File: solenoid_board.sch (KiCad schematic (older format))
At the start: 37 parts, among them J1 INPUT_ARRAY, J2 MCU_LEFT_LEGS, J3 MCU_RIGHT_LEGS, J4 Solenoid_PWR_Supply, J5 CAN_BUS, J6 SOLENOID_HEADER, Q1 PHP79NQ08LT, Q2 PHP79NQ08LT, Q3 PHP79NQ08LT, Q4 PHP79NQ08LT, Q5 PHP79NQ08LT, Q6 PHP79NQ08LT, U1 MCP2517FD-xSL, U2 CD4072B, U3 CD4072B, U4 MCP2542FDxMF, U5 74HC165, U6 74HC165, Y1 Crystal

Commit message: Swap to RS485, pre-PCB layout
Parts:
- removed C1, C2: 22pF, Capacitor_SMD:C_2010_5025Metric_Pad1.52x2.65mm_HandSolder, symbol Device:C
- removed C3, C4, C5: 0.1nF, Capacitor_SMD:C_2010_5025Metric_Pad1.52x2.65mm_HandSolder, symbol Device:C
- removed D1, D2, D3, D4, D5, D6: 1N4007, Diode_THT:D_DO-41_SOD81_P10.16mm_Horizontal, symbol Diode:1N4007
- removed J1: INPUT_ARRAY, Connector_PinHeader_2.54mm:PinHeader_1x12_P2.54mm_Vertical, symbol Connector_Generic:Conn_01x12
- removed J5: CAN_BUS, TerminalBlock:TerminalBlock_bornier-2_P5.08mm, symbol Connector_Generic:Conn_01x02
- removed J6: SOLENOID_HEADER, Connector_PinHeader_2.54mm:PinHeader_1x06_P2.54mm_Vertical, symbol Connector_Generic:Conn_01x06
- removed U1: MCP2517FD-xSL, Package_SO:SOIC-14_3.9x8.7mm_P1.27mm, symbol Interface_CAN_LIN:MCP2517FD-xSL
- removed U2, U3: CD4072B, CD4072BM96:CD4072BM96, symbol LOGIC_ICs:CD4072B
- removed U4: MCP2542FDxMF, Package_DFN_QFN:DFN-8-1EP_3x3mm_P0.65mm_EP1.55x2.4mm, symbol Interface_CAN_LIN:MCP2542FDxMF
- removed Y1: Crystal, ECS200205PXTR:XTAL_ECS-200-20-5PX-TR, symbol Device:Crystal
- added J1, J10, J11, J7, J8, J9: Screw_Terminal_01x02, TerminalBlock:TerminalBlock_bornier-2_P5.08mm, symbol Connector:Screw_Terminal_01x02
- added J5: RJ45, Connector_RJ:RJ45_Pulse_JK0654219NL_Horizontal, symbol Connector:RJ45
- added J6: Screw_Terminal_01x06, TerminalBlock:TerminalBlock_bornier-6_P5.08mm, symbol Connector:Screw_Terminal_01x06
- added R8: 10, Resistor_SMD:R_2010_5025Metric_Pad1.52x2.65mm_HandSolder, symbol Device:R
- added R9: 10k, Resistor_SMD:R_2010_5025Metric_Pad1.52x2.65mm_HandSolder, symbol Device:R
- added U1: CDSOT23-SM712, CDSOT23-SM712:CDSOT23-SM712, symbol Protection_ICs:CDSOT23-SM712
- added U4: SN65HVD72DR, sn65hvd72:SN65HVD72DR, symbol Interface_RS485:SN65HVD72DR
- R1: value 120 -> 10
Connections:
- net labels removed: RXCAN, TXCAN
- wire segments 71 -> 63
- no-connect marks 14 -> 22

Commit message: COMPLETE ROUTING!!!
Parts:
- removed R9: 10k, Resistor_SMD:R_2010_5025Metric_Pad1.52x2.65mm_HandSolder, symbol Device:R
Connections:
- net D10: now also R4.2; no longer R5.2
- net D11: now also R3.2; no longer R6.2
- net D12: now also R2.2; no longer R7.2
- net D13: no longer J1.1 (Pin_1), J1.2 (Pin_2), J10.1 (Pin_1), J10.2 (Pin_2), J11.1 (Pin_1), J11.2 (Pin_2), J7.1 (Pin_1), J7.2 (Pin_2), J8.1 (Pin_1), J8.2 (Pin_2), J9.1 (Pin_1), J9.2 (Pin_2), U5.11 (D0), U5.12 (D1), U5.13 (D2), U5.14 (D3), U5.3 (D4), U5.4 (D5), U5.5 (D6), U5.6 (D7), U6.11 (D0), U6.12 (D1), U6.13 (D2), U6.14 (D3)
- net D5: now also R7.2; no longer R2.2
- net D6: now also R6.2; no longer R3.2
- net D9: now also R5.2; no longer R4.2
- net RJ45_4: now reaches R1.1, U4.6 (A)
- net RJ45_4: now also J5.4; no longer J5.5
- net RJ45_5: now reaches R8.1, U4.7 (B)
- net RJ45_5: now also J5.5; no longer J5.4
- new net INP0_0: J1.1 (Pin_1), U5.11 (D0)
- new net INP0_1: J1.2 (Pin_2), U5.12 (D1)
- new net INP1_0: J7.1 (Pin_1), U5.13 (D2)
- new net INP1_1: J7.2 (Pin_2), U5.14 (D3)
- new net INP2_0: J8.1 (Pin_1), U5.3 (D4)
- new net INP2_1: J8.2 (Pin_2), U5.4 (D5)
- new net INP3_0: J9.1 (Pin_1), U5.5 (D6)
- new net INP3_1: J9.2 (Pin_2), U5.6 (D7)
- new net INP4_0: J10.1 (Pin_1), U6.11 (D0)
- new net INP4_1: J10.2 (Pin_2), U6.12 (D1)
- new net INP5_0: J11.1 (Pin_1), U6.13 (D2)
- new net INP5_1: J11.2 (Pin_2), U6.14 (D3)
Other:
- moved on the sheet: U5, U6

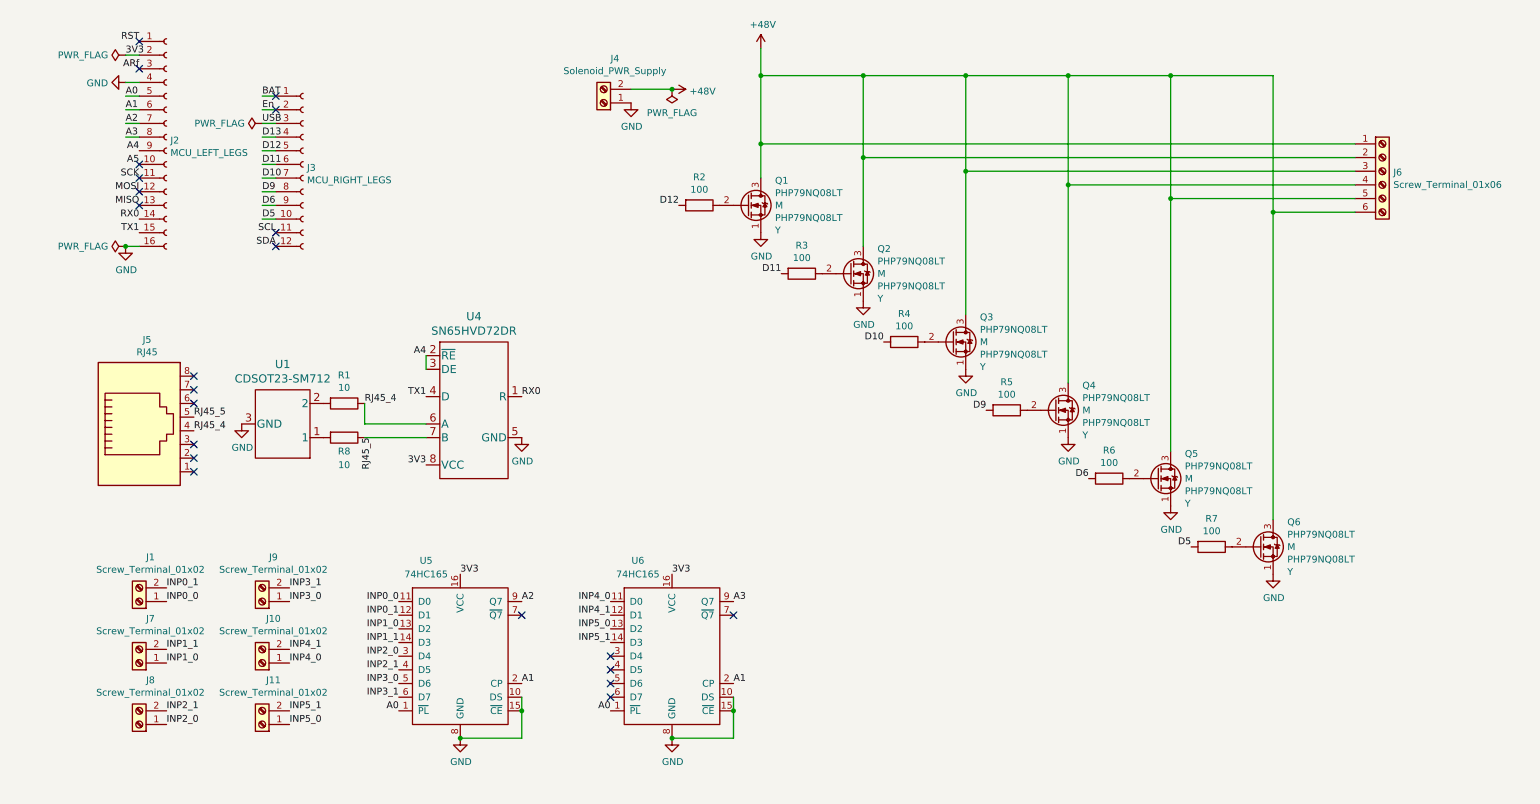
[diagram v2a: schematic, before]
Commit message: update schematic and netlist, fixing traces
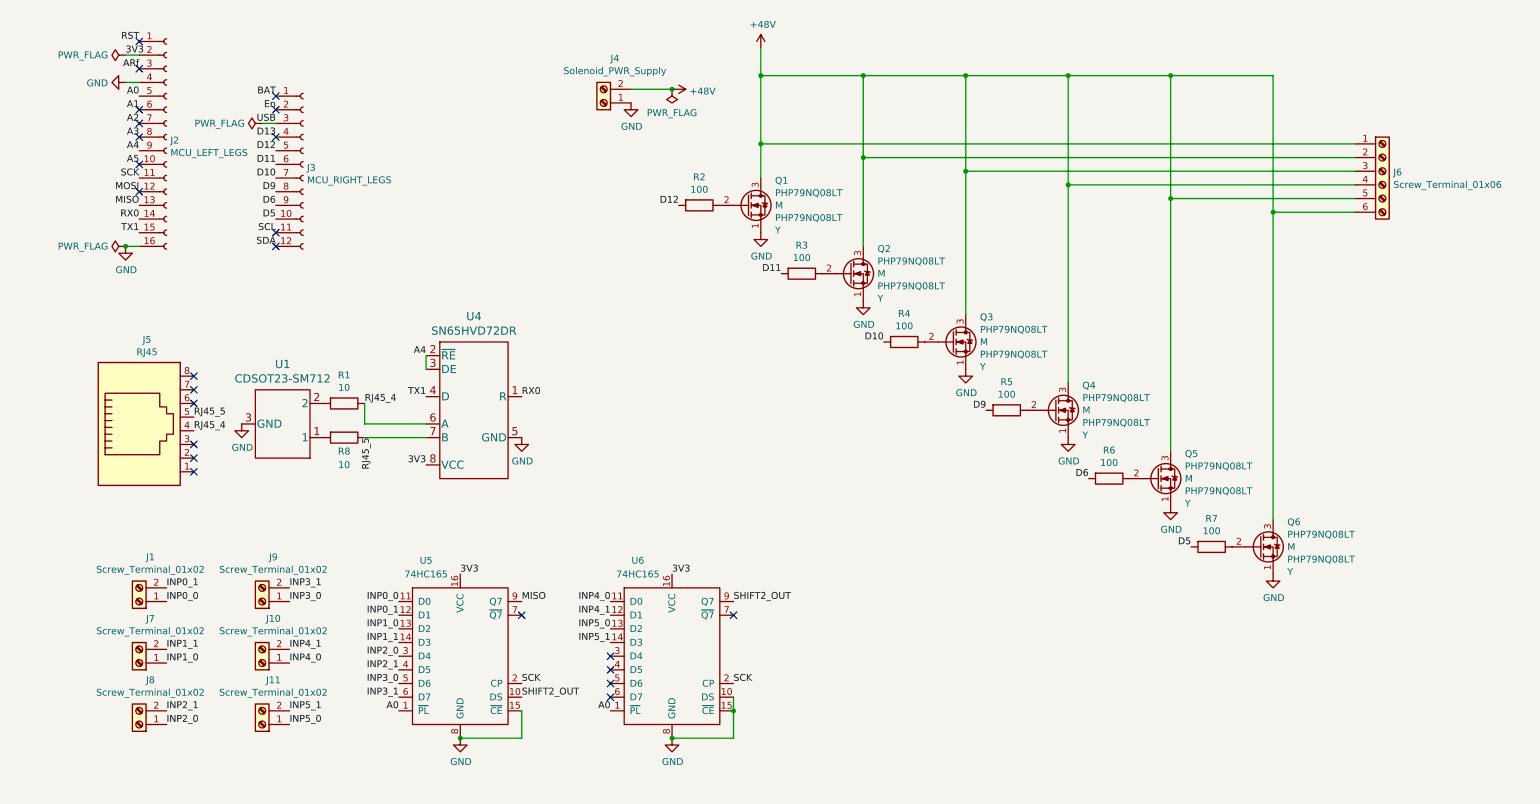
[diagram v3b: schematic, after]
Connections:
- net A1: no longer U5.2 (CP), U6.2 (CP)
- net A2: no longer U5.9 (Q7)
- net A3: no longer U6.9 (Q7)
- net GND: no longer U5.10 (DS)
- net MISO: now also U5.9 (Q7)
- net SCK: now also U5.2 (CP), U6.2 (CP)
- new net SHIFT2_OUT: U5.10 (DS), U6.9 (Q7)
- no-connect marks 22 -> 24
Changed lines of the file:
@@
 Wire Wire Line
 	1200 1000 1100 1000
-Wire Wire Line
-	1200 1100 1100 1100
-Wire Wire Line
-	1200 1200 1100 1200
 Text Label 1200 700  2    50   ~ 0
 RST
@@
 Text Label 1200 900  2    50   ~ 0
 ARf
-Text Label 1100 1100 0    50   ~ 0
+Text Label 1200 1100 2    50   ~ 0
 A0
-Text Label 1100 1200 0    50   ~ 0
+Text Label 1200 1200 2    50   ~ 0
 A1
 Wire Wire Line
-	1200 1300 1100 1300
-Wire Wire Line
-	1200 1400 1100 1400
-Wire Wire Line
 	1200 2200 1100 2200
-Text Label 1100 1300 0    50   ~ 0
+Text Label 1200 1300 2    50   ~ 0
 A2
-Text Label 1100 1400 0    50   ~ 0
-A3
 Text Label 1200 1500 2    50   ~ 0
 A4
@@
 $EndComp
 Wire Wire Line
-	2200 1100 2100 1100
-Wire Wire Line
-	2200 1200 2100 1200
-Wire Wire Line
 	2200 1300 2100 1300
-Wire Wire Line
-	2200 1400 2100 1400
-Wire Wire Line
-	2200 1500 2100 1500
-Wire Wire Line
-	2200 1600 2100 1600
-Wire Wire Line
-	2200 1700 2100 1700
-Wire Wire Line
-	2200 1800 2100 1800
-Wire Wire Line
-	2200 1900 2100 1900
-Wire Wire Line
-	2200 2000 2100 2000
-Text Label 2100 1100 0    50   ~ 0
+Text Label 2200 1100 2    50   ~ 0
 BAT
-Text Label 2100 1200 0    50   ~ 0
+Text Label 2200 1200 2    50   ~ 0
 En
-Text Label 2100 1300 0    50   ~ 0
+Text Label 2200 1300 2    50   ~ 0
 USB
-Text Label 2100 1400 0    50   ~ 0
-D13
-Text Label 2100 1500 0    50   ~ 0
+Text Label 2200 1500 2    50   ~ 0
 D12
-Text Label 2100 1600 0    50   ~ 0
+Text Label 2200 1600 2    50   ~ 0
 D11
-Text Label 2100 1700 0    50   ~ 0
+Text Label 2200 1700 2    50   ~ 0
 D10
-Text Label 2100 1800 0    50   ~ 0
+Text Label 2200 1800 2    50   ~ 0
 D9
-Text Label 2100 1900 0    50   ~ 0
+Text Label 2200 1900 2    50   ~ 0
 D6
-Text Label 2100 2000 0    50   ~ 0
+Text Label 2200 2000 2    50   ~ 0
 D5
 Text Label 2200 2100 2    50   ~ 0
@@
 Text Label 3100 5400 2    50   ~ 0
 INP3_0
-Text Label 4000 4800 0    50   ~ 0
-A2
-Wire Wire Line
-	4000 5500 4000 5600
 Text Label 3100 5500 2    50   ~ 0
 INP3_1
@@
 A0
 Text Label 4000 5400 0    50   ~ 0
-A1
+SCK
 $Comp
 L LOGIC_ICs:74HC165 U6
@@
 A0
 Text Label 5550 5400 0    50   ~ 0
-A1
+SCK
 Text Label 5550 4800 0    50   ~ 0
-A3
+SHIFT2_OUT
 Wire Wire Line
 	5550 5500 5550 5600
@@
 Wire Wire Line
 	4000 5800 3550 5800
-Connection ~ 4000 5600
 Connection ~ 3550 5800
 $Comp
@@
 Text Label 4000 3300 0    50   ~ 0
 RX0
-NoConn ~ 1200 1700
 NoConn ~ 1200 1800
-NoConn ~ 1200 1900
 Text Label 3300 3300 2    50   ~ 0
 TX1
@@
 Text Label 2900 3600 3    50   ~ 0
 RJ45_5
+Text Label 4000 5500 0    50   ~ 0
+SHIFT2_OUT
+Text Label 4000 4800 0    50   ~ 0
+MISO
+Text Label 1200 1400 2    50   ~ 0
+A3
+NoConn ~ 1200 1400
+NoConn ~ 1200 1300
+NoConn ~ 1200 1200
+NoConn ~ 2200 1400
+Text Label 2200 1400 2    50   ~ 0
+D13
 $EndSCHEMATC

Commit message: Finish routing
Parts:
- added J12: Screw_Terminal_01x06, TerminalBlock:TerminalBlock_bornier-6_P5.08mm, symbol Connector:Screw_Terminal_01x06
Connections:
- net +48V: now also J12.1 (Pin_1), J12.3 (Pin_3), J12.5 (Pin_5); no longer J6.2 (Pin_2), J6.4 (Pin_4), J6.6 (Pin_6), Q1.3 (D), Q2.3 (D), Q3.3 (D), Q4.3 (D), Q5.3 (D), Q6.3 (D)
- new net: J6.2 (Pin_2), Q1.3 (D)
- new net: J6.4 (Pin_4), Q2.3 (D)
- new net: J6.6 (Pin_6), Q3.3 (D)
- new net: J12.2 (Pin_2), Q4.3 (D)
- new net: J12.4 (Pin_4), Q5.3 (D)
- new net: J12.6 (Pin_6), Q6.3 (D)
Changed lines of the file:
@@
 Wire Wire Line
 	5750 950  5750 750
-Wire Wire Line
-	5750 1450 5750 1700
-Connection ~ 5750 1450
 $Comp
 L MOSFETs:PHP79NQ08LT Q2
@@
 $EndComp
 Wire Wire Line
-	6500 1550 6500 2200
-Connection ~ 6500 1550
-Wire Wire Line
-	7250 1650 7250 2700
-Connection ~ 7250 1650
-Wire Wire Line
-	8000 1750 8000 3200
-Connection ~ 8000 1750
-Wire Wire Line
 	5750 1450 10100 1450
-Wire Wire Line
-	6500 1550 10100 1550
-Wire Wire Line
-	7250 1650 10100 1650
-Wire Wire Line
-	8000 1750 10100 1750
 $Comp
 L Device:R R6
@@
 	1    0    0    -1
 $EndComp
-Wire Wire Line
-	8750 1850 10100 1850
-Wire Wire Line
-	8750 1850 8750 3700
-Connection ~ 8750 1850
-Wire Wire Line
-	10100 1950 9500 1950
-Connection ~ 9500 1950
-Wire Wire Line
-	9500 1950 9500 4200
 Text Label 5900 2400 2    50   ~ 0
 D11
@@
 	5750 950  5750 1450
 Connection ~ 5750 950
-Wire Wire Line
-	6500 950  6500 1550
 Connection ~ 6500 950
 Wire Wire Line
 	6500 950  7250 950
-Wire Wire Line
-	7250 950  7250 1650
 Connection ~ 7250 950
 Wire Wire Line
 	7250 950  8000 950
-Wire Wire Line
-	8000 950  8000 1750
 Connection ~ 8000 950
 Wire Wire Line
 	8000 950  8750 950
-Wire Wire Line
-	8750 950  8750 1850
 Connection ~ 8750 950
 Wire Wire Line
 	8750 950  9500 950
-Wire Wire Line
-	9500 950  9500 1950
 $Comp
 L power:GND #PWR04
@@
 NoConn ~ 1600 3250
 NoConn ~ 1600 3150
-$Comp
-L Connector:Screw_Terminal_01x06 J6
-U 1 1 5E21E9C4
-P 10300 1650
-F 0 "J6" H 10380 1642 50  0000 L CNN
-F 1 "Screw_Terminal_01x06" H 10380 1551 50  0000 L CNN
-F 2 "TerminalBlock:TerminalBlock_bornier-6_P5.08mm" H 10300 1650 50  0001 C CNN
-F 3 "~" H 10300 1650 50  0001 C CNN
-	1    10300 1650
-	1    0    0    -1
-$EndComp
 $Comp
 L Connector:Screw_Terminal_01x02 J1
@@
 Text Label 2200 1400 2    50   ~ 0
 D13
+Wire Wire Line
+	5750 1550 5750 1700
+Wire Wire Line
+	5750 1550 10100 1550
+Wire Wire Line
+	6500 950  6500 1650
+Wire Wire Line
+	6500 1750 6500 2200
+Wire Wire Line
+	7250 950  7250 1850
+Wire Wire Line
+	6500 1650 10100 1650
+Wire Wire Line
+	8000 950  8000 2050
+Wire Wire Line
+	6500 1750 10100 1750
+Wire Wire Line
+	7250 1850 10100 1850
+Wire Wire Line
+	8750 950  8750 2250
+Wire Wire Line
+	7250 1950 7250 2700
+Wire Wire Line
+	7250 1950 10100 1950
+Wire Wire Line
+	9500 950  9500 2450
+Wire Wire Line
+	10100 2050 8000 2050
+Wire Wire Line
+	10100 2150 8000 2150
+Wire Wire Line
+	8000 2150 8000 3200
+Wire Wire Line
+	10100 2250 8750 2250
+Wire Wire Line
+	10100 2350 8750 2350
+Wire Wire Line
+	8750 2350 8750 3700
+Wire Wire Line
+	10100 2450 9500 2450
+Wire Wire Line
+	10100 2550 9500 2550
+Wire Wire Line
+	9500 2550 9500 4200
+$Comp
+L Connector:Screw_Terminal_01x06 J6
+U 1 1 5E363393
+P 10300 1650
+F 0 "J6" H 10380 1642 50  0000 L CNN
+F 1 "Screw_Terminal_01x06" H 10380 1551 50  0000 L CNN
+F 2 "TerminalBlock:TerminalBlock_bornier-6_P5.08mm" H 10300 1650 50  0001 C CNN
+F 3 "~" H 10300 1650 50  0001 C CNN
+	1    10300 1650
+	1    0    0    -1
+$EndComp
+$Comp
+L Connector:Screw_Terminal_01x06 J12
+U 1 1 5E364567
+P 10300 2250
+F 0 "J12" H 10380 2242 50  0000 L CNN
+F 1 "Screw_Terminal_01x06" H 10380 2151 50  0000 L CNN
+F 2 "TerminalBlock:TerminalBlock_bornier-6_P5.08mm" H 10300 2250 50  0001 C CNN
+F 3 "~" H 10300 2250 50  0001 C CNN
+	1    10300 2250
+	1    0    0    -1
+$EndComp
 $EndSCHEMATC

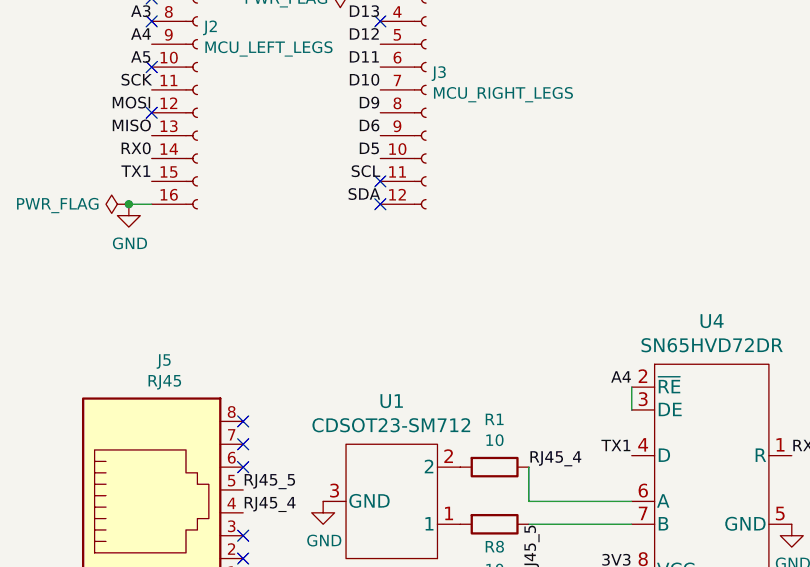
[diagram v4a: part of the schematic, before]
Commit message: Add grounding pin
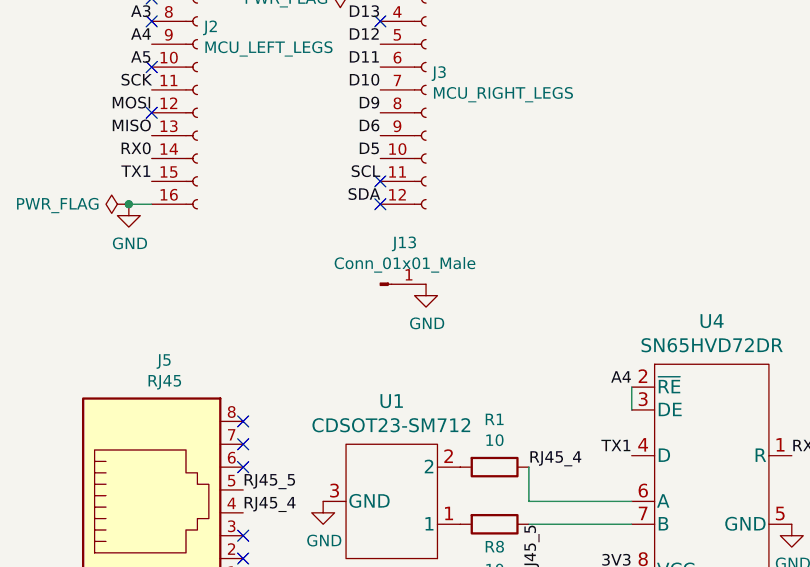
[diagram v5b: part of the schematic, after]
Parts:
- added J13: Conn_01x01_Male, Connector_PinHeader_2.54mm:PinHeader_1x01_P2.54mm_Vertical, symbol Connector:Conn_01x01_Male
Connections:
- net GND: now also J13.1 (Pin_1)
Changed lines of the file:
@@
+	1    0    0    -1
+$EndComp
+$Comp
+L Connector:Conn_01x01_Male J13
+U 1 1 5E371F26
+P 2200 2550
+F 0 "J13" H 2308 2731 50  0000 C CNN
+F 1 "Conn_01x01_Male" H 2308 2640 50  0000 C CNN
+F 2 "Connector_PinHeader_2.54mm:PinHeader_1x01_P2.54mm_Vertical" H 2200 2550 50  0001 C CNN
+F 3 "~" H 2200 2550 50  0001 C CNN
+	1    2200 2550
+	1    0    0    -1
+$EndComp
+$Comp
+L power:GND #PWR05
+U 1 1 5E376948
+P 2400 2550
+F 0 "#PWR05" H 2400 2300 50  0001 C CNN
+F 1 "GND" H 2405 2377 50  0000 C CNN
+F 2 "" H 2400 2550 50  0001 C CNN
+F 3 "" H 2400 2550 50  0001 C CNN
+	1    2400 2550
 	1    0    0    -1
 $EndComp
